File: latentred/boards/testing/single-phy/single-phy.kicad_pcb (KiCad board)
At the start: 4 copper layers, 76.8 x 34.2 mm, 80 parts, among them J1 XILINX_JTAG, J2 RJ45, J3 QSH-030-01-L-D-A, U1 DP83867, U2 25MHZ_TBD, U3 BEL_FUSE_S558-5999-M8-F, U4 LTC3374-QFN

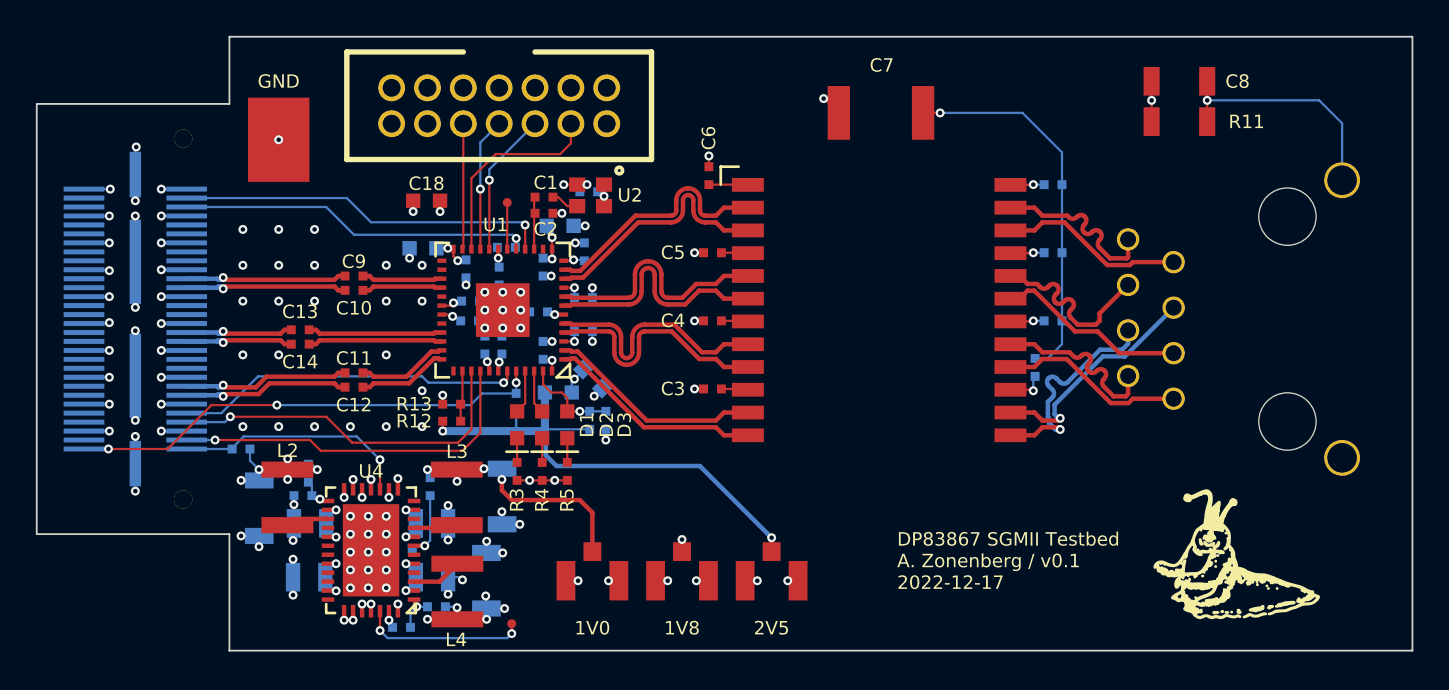
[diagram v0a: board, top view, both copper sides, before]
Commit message: single-phy: updated for v0.2 with fixed RJ45 pinout, removed SGMII clock pair, moved digital IO to 1.8V
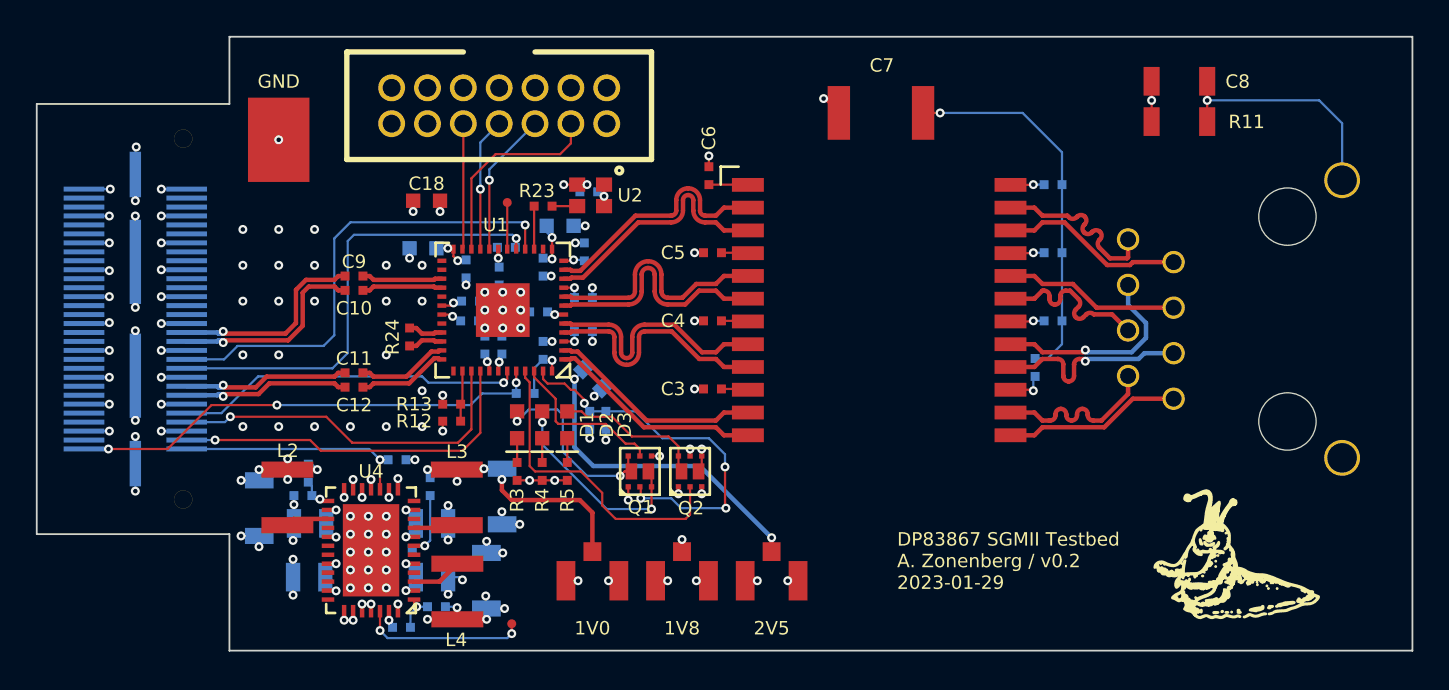
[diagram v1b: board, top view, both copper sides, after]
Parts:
- removed C1, C2: 27p, azonenberg_pcb:EIA_0402_CAP_NOSILK
- removed C13, C14: 0.1 uF, azonenberg_pcb:EIA_0402_CAP_NOSILK
- removed L1: FERRITE_600R, azonenberg_pcb:EIA_0603_INDUCTOR_NOSILK
- added Q1: SSM6N58NU, azonenberg_pcb:DFN_6_0.65MM_2x2MM_GDS, F.Cu at (78.2, 79.5)
- added Q2: SSM6N58NU, azonenberg_pcb:DFN_6_0.65MM_2x2MM_GDS, F.Cu at (81.0, 79.5)
- added R23: 33, azonenberg_pcb:EIA_0402_RES_NOSILK, F.Cu at (72.8, 64.7)
- added R24: 100, azonenberg_pcb:EIA_0402_RES_NOSILK, F.Cu at (65.3, 72.0)
- moved R22 8.72 mm to (64.6, 78.8)
- moved R1 0.71 mm to (71.8, 75.2), turned to 180 degrees
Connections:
- C15 pad 1: /A2V5 -> /2V5
- C18 pad 1: /2V5 -> /1V8
- C19 pad 1: /A2V5 -> /2V5
- C22 pad 1: /2V5 -> /1V8
- C25 pad 1: /2V5 -> /1V8
- C26 pad 1: /A2V5 -> /2V5
- C28 pad 1: /2V5 -> /1V8
- C30 pad 1: /2V5 -> /1V8
- D1 pad 2: /LED_2 -> Net-(D1-Pad2)
- D2 pad 2: /LED_1 -> Net-(D2-Pad2)
- D3 pad 2: /LED_0 -> Net-(D3-Pad2)
- J1 pad 2: /2V5 -> /1V8
- J2 pad 1: /ETH_MDI_B_P -> /ETH_MDI_A_P
- J2 pad 2: /ETH_MDI_B_N -> /ETH_MDI_A_N
- J2 pad 3: /ETH_MDI_C_P -> /ETH_MDI_B_P
- J2 pad 4: /ETH_MDI_A_P -> /ETH_MDI_C_P
- J2 pad 5: /ETH_MDI_A_N -> /ETH_MDI_C_N
- J2 pad 6: /ETH_MDI_C_N -> /ETH_MDI_B_N
- J3 pad 20: unconnected-(J3-Pad20) -> /MGMT_MDIO
- J3 pad 22: unconnected-(J3-Pad22) -> /MGMT_MDC
- J3 pad 26: /SGMII_CLKOUT_N -> /SGMII_TX_N
- J3 pad 28: /SGMII_CLKOUT_P -> /SGMII_TX_P
- J3 pad 38: /SGMII_TX_N -> unconnected-(J3-Pad38)
- J3 pad 40: /SGMII_TX_P -> unconnected-(J3-Pad40)
- J3 pad 56: /MGMT_MDIO -> unconnected-(J3-Pad56)
- J3 pad 58: /MGMT_MDC -> unconnected-(J3-Pad58)
- R1 pad 1: /2V5 -> /1V8
- R12 pad 2: /2V5 -> /1V8
- R14 pad 2: /2V5 -> /1V8
- R22 pad 2: /2V5 -> /1V8
- R6 pad 2: /2V5 -> /1V8
- U1 pad 15: /PHY_CLK_25MHZ_DIV -> /PHY_CLK_25MHZ
- U1 pad 19: /2V5 -> /1V8
- U1 pad 3: /A2V5 -> /2V5
- U1 pad 30: /2V5 -> /1V8
- U1 pad 41: /2V5 -> /1V8
- U1 pad 9: /A2V5 -> /2V5
- U2 pad 1: /2V5 -> /1V8
- U2 pad 3: /PHY_CLK_25MHZ -> Net-(U2-Pad3)
- U2 pad 4: /2V5 -> /1V8
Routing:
- net /1V8: track 56.3 -> 105.1 mm, vias 9 -> 17
- net /2V5: track 88.8 -> 57.1 mm, vias 12 -> 9
- net /LED_0: track 5.31 -> 21.1 mm, vias 1 -> 4
- net /LED_2: track 2.44 -> 17.6 mm
- net Net-(D2-Pad2): track 0.00 -> 11.4 mm, vias 0 -> 2
- net /GND: track 397.1 -> 408.1 mm, vias 123 -> 128
- net Net-(D1-Pad2): track 0.00 -> 10.7 mm, vias 0 -> 2
- net /A2V5: track 8.88 -> 0.00 mm, vias 3 -> 0
- net Net-(D3-Pad2): track 0.00 -> 8.23 mm
- net /LED_1: track 2.44 -> 9.03 mm
- net /MGMT_MDIO: track 20.2 -> 26.3 mm
- net /SGMII_CLKOUT_P: track 6.05 -> 0.00 mm, vias 1 -> 0
- net /SGMII_CLKOUT_N: track 6.05 -> 0.00 mm, vias 1 -> 0
- net /MGMT_MDC: track 20.9 -> 26.6 mm
- net /SGMII_CLKOUT_AC_P: track 7.51 -> 1.96 mm
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- removed copper zone on In2.Cu, net /A2V5
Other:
- board text added: "DP83867 SGMII Testbed A. Zonenberg / v0.2 2023-01-29"
- board text removed: "DP83867 SGMII Testbed A. Zonenberg / v0.1 2022-12-17"

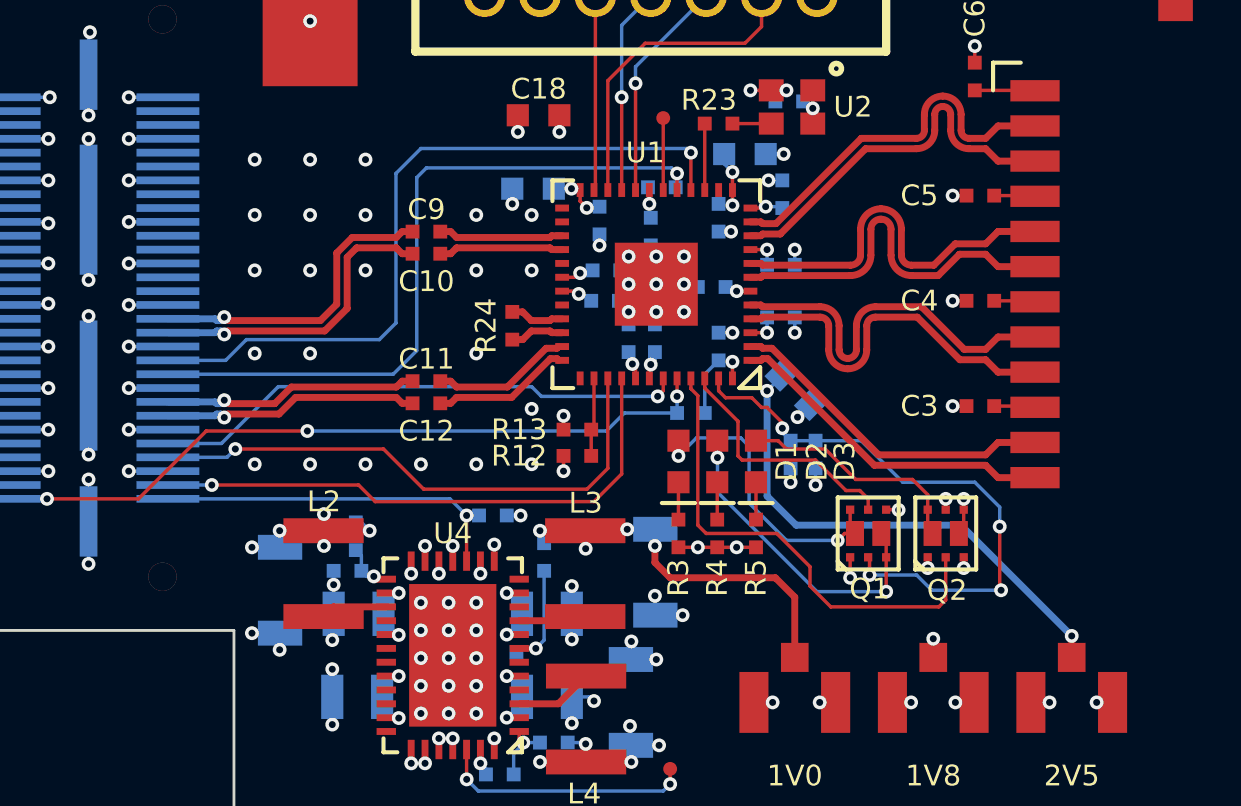
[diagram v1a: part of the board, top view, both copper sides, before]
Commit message: Fixed incorrect LED level shifter connections
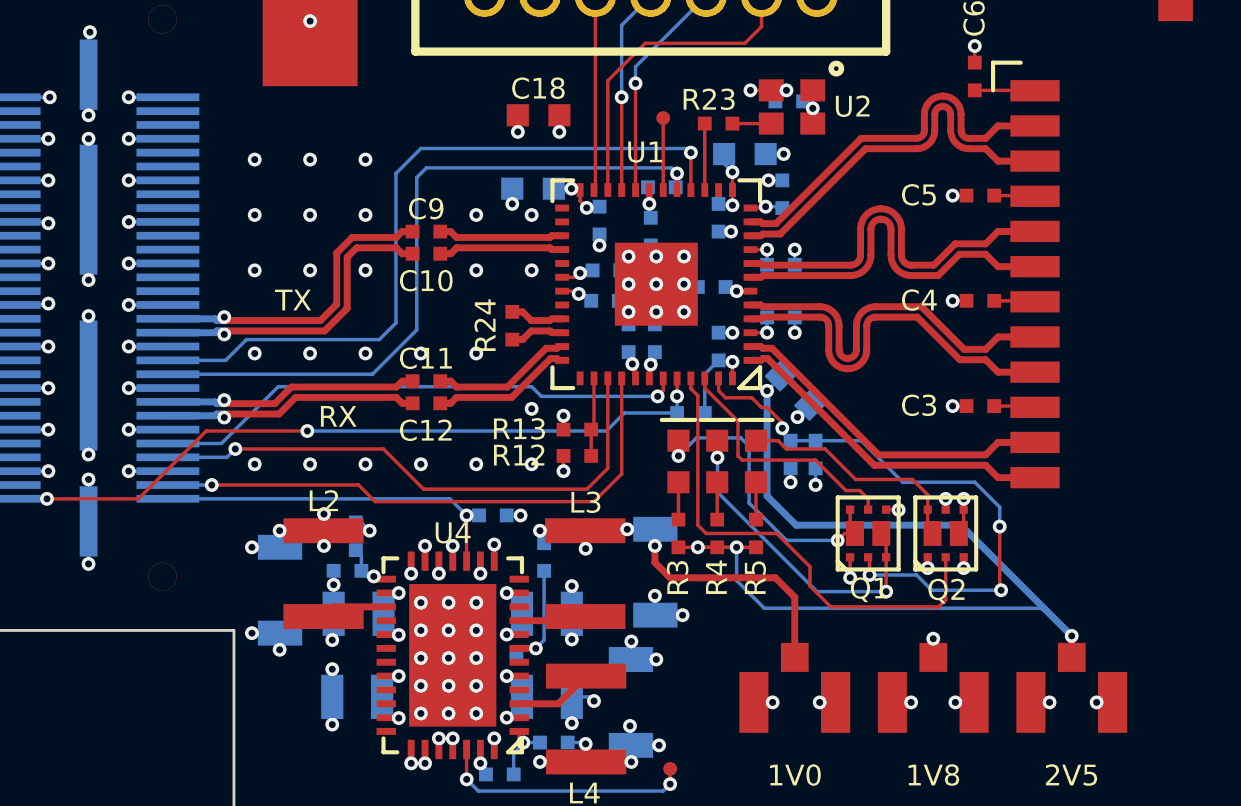
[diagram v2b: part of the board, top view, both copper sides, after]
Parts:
- turned D1 to -90 degrees
- turned D2 to -90 degrees
- turned D3 to -90 degrees
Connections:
- D1 pad 1: Net-(D1-Pad1) -> Net-(Q1-PadD1)
- D2 pad 1: Net-(D2-Pad1) -> Net-(Q1-PadD2)
- D2 pad 2: Net-(D2-Pad2) -> Net-(R4-Pad1)
- D3 pad 1: Net-(D3-Pad1) -> Net-(Q2-PadD1)
- Q1 pad D1: Net-(D1-Pad2) -> Net-(Q1-PadD1)
- Q1 pad D2: Net-(D2-Pad2) -> Net-(Q1-PadD2)
- Q2 pad D1: Net-(D3-Pad2) -> Net-(Q2-PadD1)
- R3 pad 1: Net-(D1-Pad1) -> Net-(D1-Pad2)
- R3 pad 2: /GND -> /2V5
- R4 pad 1: Net-(D2-Pad1) -> Net-(R4-Pad1)
- R4 pad 2: /GND -> /2V5
- R5 pad 1: Net-(D3-Pad1) -> Net-(D3-Pad2)
- R5 pad 2: /GND -> /2V5
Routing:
- net /2V5: track 57.1 -> 74.0 mm, vias 9 -> 11
- net Net-(Q1-PadD2): track 0.00 -> 11.4 mm, vias 0 -> 2
- net Net-(D2-Pad2): track 11.4 -> 0.00 mm, vias 2 -> 0
- net Net-(Q1-PadD1): track 0.00 -> 10.7 mm, vias 0 -> 2
- net Net-(D1-Pad2): track 10.7 -> 1.35 mm, vias 2 -> 0
- net Net-(Q2-PadD1): track 0.00 -> 8.23 mm
- net Net-(D3-Pad2): track 8.23 -> 1.35 mm
- net /GND: track 408.1 -> 411.3 mm
- net Net-(R4-Pad1): track 0.00 -> 1.35 mm
- net Net-(D3-Pad1): track 1.35 -> 0.00 mm
- net Net-(D2-Pad1): track 1.35 -> 0.00 mm
- net Net-(D1-Pad1): track 1.35 -> 0.00 mm
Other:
- board text added: "RX"
- board text added: "TX"
